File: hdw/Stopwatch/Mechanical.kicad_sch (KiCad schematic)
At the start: 12 parts

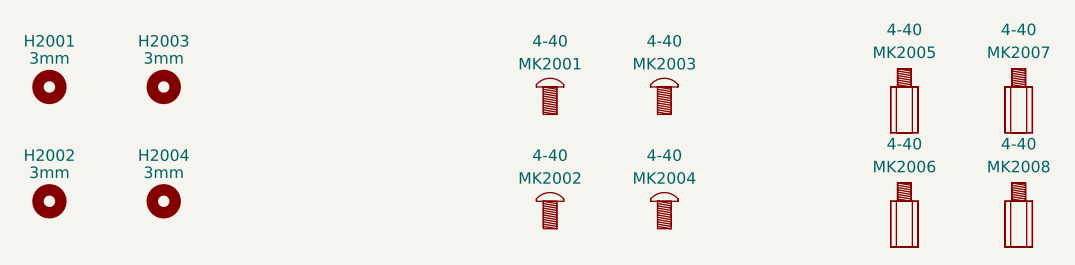
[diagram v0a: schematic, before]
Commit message: adjusted stage sheet
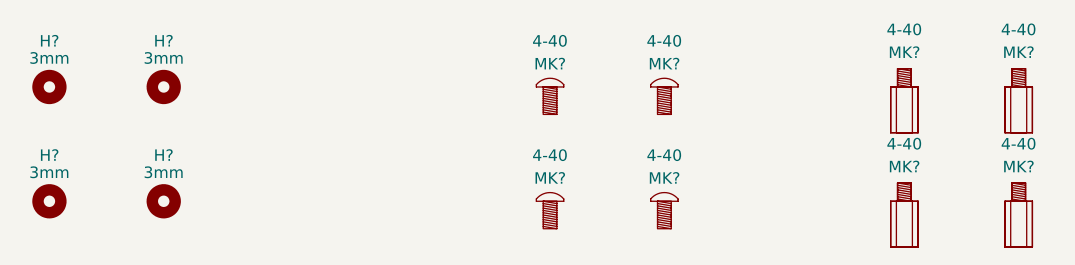
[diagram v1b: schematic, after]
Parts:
- renumbered H2001 to H?, H2003 to H?, H2002 to H?, H2004 to H?, MK2001 to MK?, MK2003 to MK?, MK2002 to MK?, MK2004 to MK?, MK2005 to MK?, MK2007 to MK?, MK2006 to MK?, MK2008 to MK?
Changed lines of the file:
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@@
   (symbol (lib_id "Mechanical:MountingHole") (at 42.164 44.45 0) (unit 1)
     (in_bom yes) (on_board yes) (dnp no)
-    (property "Reference" "H2001" (at 42.164 39.37 0)
+    (property "Reference" "H?" (at 42.164 39.37 0)
       (effects (font (size 1.27 1.27)))
     )
@@
       (project "Stopwatch"
         (path "/c0d2575b-aec2-49ed-8c32-97fe6e68824c/00000000-0000-0000-0000-00005d77c1ea"
-          (reference "H2001") (unit 1)
+          (reference "H?") (unit 1)
         )
       )
@@
   (symbol (lib_id "Mechanical:MountingHole") (at 54.864 44.45 0) (unit 1)
     (in_bom yes) (on_board yes) (dnp no)
-    (property "Reference" "H2003" (at 54.864 39.37 0)
+    (property "Reference" "H?" (at 54.864 39.37 0)
       (effects (font (size 1.27 1.27)))
     )
@@
       (project "Stopwatch"
         (path "/c0d2575b-aec2-49ed-8c32-97fe6e68824c/00000000-0000-0000-0000-00005d77c1ea"
-          (reference "H2003") (unit 1)
+          (reference "H?") (unit 1)
         )
       )
@@
   (symbol (lib_id "Mechanical:MountingHole") (at 42.164 57.15 0) (unit 1)
     (in_bom yes) (on_board yes) (dnp no)
-    (property "Reference" "H2002" (at 42.164 52.07 0)
+    (property "Reference" "H?" (at 42.164 52.07 0)
       (effects (font (size 1.27 1.27)))
     )
@@
       (project "Stopwatch"
         (path "/c0d2575b-aec2-49ed-8c32-97fe6e68824c/00000000-0000-0000-0000-00005d77c1ea"
-          (reference "H2002") (unit 1)
+          (reference "H?") (unit 1)
         )
       )
@@
   (symbol (lib_id "Mechanical:MountingHole") (at 54.864 57.15 0) (unit 1)
     (in_bom yes) (on_board yes) (dnp no)
-    (property "Reference" "H2004" (at 54.864 52.07 0)
+    (property "Reference" "H?" (at 54.864 52.07 0)
       (effects (font (size 1.27 1.27)))
     )
@@
       (project "Stopwatch"
         (path "/c0d2575b-aec2-49ed-8c32-97fe6e68824c/00000000-0000-0000-0000-00005d77c1ea"
-          (reference "H2004") (unit 1)
+          (reference "H?") (unit 1)
         )
       )
@@
   (symbol (lib_id "Custom_Library:Screw") (at 97.79 44.45 0) (unit 1)
     (in_bom yes) (on_board yes) (dnp no)
-    (property "Reference" "MK2001" (at 97.79 41.91 0)
+    (property "Reference" "MK?" (at 97.79 41.91 0)
       (effects (font (size 1.27 1.27)))
     )
@@
       (project "Stopwatch"
         (path "/c0d2575b-aec2-49ed-8c32-97fe6e68824c/00000000-0000-0000-0000-00005d77c1ea"
-          (reference "MK2001") (unit 1)
+          (reference "MK?") (unit 1)
         )
       )
@@
   (symbol (lib_id "Custom_Library:Screw") (at 110.49 44.45 0) (unit 1)
     (in_bom yes) (on_board yes) (dnp no)
-    (property "Reference" "MK2003" (at 110.49 41.91 0)
+    (property "Reference" "MK?" (at 110.49 41.91 0)
       (effects (font (size 1.27 1.27)))
     )
@@
       (project "Stopwatch"
         (path "/c0d2575b-aec2-49ed-8c32-97fe6e68824c/00000000-0000-0000-0000-00005d77c1ea"
-          (reference "MK2003") (unit 1)
+          (reference "MK?") (unit 1)
         )
       )
@@
   (symbol (lib_id "Custom_Library:Screw") (at 97.79 57.15 0) (unit 1)
     (in_bom yes) (on_board yes) (dnp no)
-    (property "Reference" "MK2002" (at 97.79 54.61 0)
+    (property "Reference" "MK?" (at 97.79 54.61 0)
       (effects (font (size 1.27 1.27)))
     )
@@
       (project "Stopwatch"
         (path "/c0d2575b-aec2-49ed-8c32-97fe6e68824c/00000000-0000-0000-0000-00005d77c1ea"
-          (reference "MK2002") (unit 1)
+          (reference "MK?") (unit 1)
         )
       )
@@
   (symbol (lib_id "Custom_Library:Screw") (at 110.49 57.15 0) (unit 1)
     (in_bom yes) (on_board yes) (dnp no)
-    (property "Reference" "MK2004" (at 110.49 54.61 0)
+    (property "Reference" "MK?" (at 110.49 54.61 0)
       (effects (font (size 1.27 1.27)))
     )
@@
       (project "Stopwatch"
         (path "/c0d2575b-aec2-49ed-8c32-97fe6e68824c/00000000-0000-0000-0000-00005d77c1ea"
-          (reference "MK2004") (unit 1)
+          (reference "MK?") (unit 1)
         )
       )
@@
   (symbol (lib_id "Custom_Library:Standoff") (at 137.16 44.45 0) (unit 1)
     (in_bom yes) (on_board yes) (dnp no)
-    (property "Reference" "MK2005" (at 137.16 40.64 0)
+    (property "Reference" "MK?" (at 137.16 40.64 0)
       (effects (font (size 1.27 1.27)))
     )
@@
       (project "Stopwatch"
         (path "/c0d2575b-aec2-49ed-8c32-97fe6e68824c/00000000-0000-0000-0000-00005d77c1ea"
-          (reference "MK2005") (unit 1)
+          (reference "MK?") (unit 1)
         )
       )
@@
   (symbol (lib_id "Custom_Library:Standoff") (at 149.86 44.45 0) (unit 1)
     (in_bom yes) (on_board yes) (dnp no)
-    (property "Reference" "MK2007" (at 149.86 40.64 0)
+    (property "Reference" "MK?" (at 149.86 40.64 0)
       (effects (font (size 1.27 1.27)))
     )
@@
       (project "Stopwatch"
         (path "/c0d2575b-aec2-49ed-8c32-97fe6e68824c/00000000-0000-0000-0000-00005d77c1ea"
-          (reference "MK2007") (unit 1)
+          (reference "MK?") (unit 1)
         )
       )
@@
   (symbol (lib_id "Custom_Library:Standoff") (at 137.16 57.15 0) (unit 1)
     (in_bom yes) (on_board yes) (dnp no)
-    (property "Reference" "MK2006" (at 137.16 53.34 0)
+    (property "Reference" "MK?" (at 137.16 53.34 0)
       (effects (font (size 1.27 1.27)))
     )
@@
       (project "Stopwatch"
         (path "/c0d2575b-aec2-49ed-8c32-97fe6e68824c/00000000-0000-0000-0000-00005d77c1ea"
-          (reference "MK2006") (unit 1)
+          (reference "MK?") (unit 1)
         )
       )
@@
   (symbol (lib_id "Custom_Library:Standoff") (at 149.86 57.15 0) (unit 1)
     (in_bom yes) (on_board yes) (dnp no)
-    (property "Reference" "MK2008" (at 149.86 53.34 0)
+    (property "Reference" "MK?" (at 149.86 53.34 0)
       (effects (font (size 1.27 1.27)))
     )
@@
       (project "Stopwatch"
         (path "/c0d2575b-aec2-49ed-8c32-97fe6e68824c/00000000-0000-0000-0000-00005d77c1ea"
-          (reference "MK2008") (unit 1)
-        )
-      )
+          (reference "MK?") (unit 1)
+        )
+      )

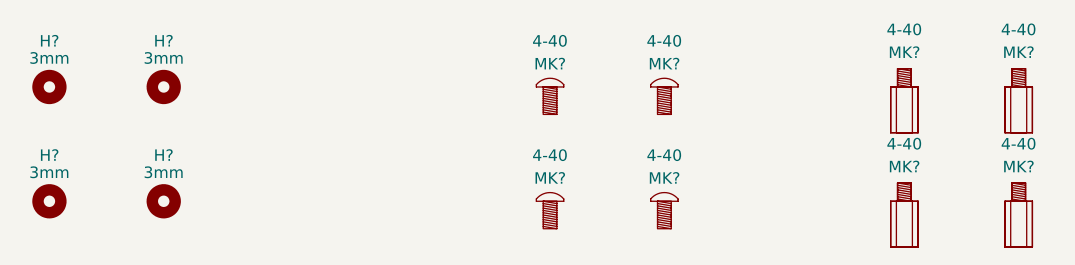
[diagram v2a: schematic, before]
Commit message: added proper power sequencing, discharge
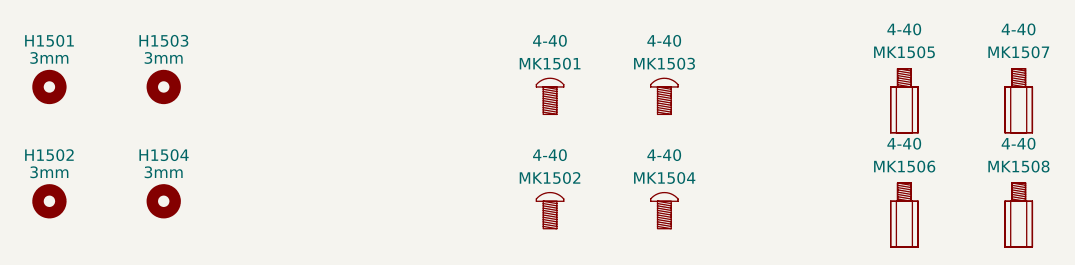
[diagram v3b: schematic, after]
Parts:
- gave numbers to parts that had none: 12
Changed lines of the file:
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@@
   (symbol (lib_id "Mechanical:MountingHole") (at 42.164 44.45 0) (unit 1)
     (in_bom yes) (on_board yes) (dnp no)
-    (property "Reference" "H?" (at 42.164 39.37 0)
+    (property "Reference" "H1501" (at 42.164 39.37 0)
       (effects (font (size 1.27 1.27)))
     )
@@
       (project "Stopwatch"
         (path "/c0d2575b-aec2-49ed-8c32-97fe6e68824c/00000000-0000-0000-0000-00005d77c1ea"
-          (reference "H?") (unit 1)
+          (reference "H1501") (unit 1)
         )
       )
@@
   (symbol (lib_id "Mechanical:MountingHole") (at 54.864 44.45 0) (unit 1)
     (in_bom yes) (on_board yes) (dnp no)
-    (property "Reference" "H?" (at 54.864 39.37 0)
+    (property "Reference" "H1503" (at 54.864 39.37 0)
       (effects (font (size 1.27 1.27)))
     )
@@
       (project "Stopwatch"
         (path "/c0d2575b-aec2-49ed-8c32-97fe6e68824c/00000000-0000-0000-0000-00005d77c1ea"
-          (reference "H?") (unit 1)
+          (reference "H1503") (unit 1)
         )
       )
@@
   (symbol (lib_id "Mechanical:MountingHole") (at 42.164 57.15 0) (unit 1)
     (in_bom yes) (on_board yes) (dnp no)
-    (property "Reference" "H?" (at 42.164 52.07 0)
+    (property "Reference" "H1502" (at 42.164 52.07 0)
       (effects (font (size 1.27 1.27)))
     )
@@
       (project "Stopwatch"
         (path "/c0d2575b-aec2-49ed-8c32-97fe6e68824c/00000000-0000-0000-0000-00005d77c1ea"
-          (reference "H?") (unit 1)
+          (reference "H1502") (unit 1)
         )
       )
@@
   (symbol (lib_id "Mechanical:MountingHole") (at 54.864 57.15 0) (unit 1)
     (in_bom yes) (on_board yes) (dnp no)
-    (property "Reference" "H?" (at 54.864 52.07 0)
+    (property "Reference" "H1504" (at 54.864 52.07 0)
       (effects (font (size 1.27 1.27)))
     )
@@
       (project "Stopwatch"
         (path "/c0d2575b-aec2-49ed-8c32-97fe6e68824c/00000000-0000-0000-0000-00005d77c1ea"
-          (reference "H?") (unit 1)
+          (reference "H1504") (unit 1)
         )
       )
@@
   (symbol (lib_id "Custom_Library:Screw") (at 97.79 44.45 0) (unit 1)
     (in_bom yes) (on_board yes) (dnp no)
-    (property "Reference" "MK?" (at 97.79 41.91 0)
+    (property "Reference" "MK1501" (at 97.79 41.91 0)
       (effects (font (size 1.27 1.27)))
     )
@@
       (project "Stopwatch"
         (path "/c0d2575b-aec2-49ed-8c32-97fe6e68824c/00000000-0000-0000-0000-00005d77c1ea"
-          (reference "MK?") (unit 1)
+          (reference "MK1501") (unit 1)
         )
       )
@@
   (symbol (lib_id "Custom_Library:Screw") (at 110.49 44.45 0) (unit 1)
     (in_bom yes) (on_board yes) (dnp no)
-    (property "Reference" "MK?" (at 110.49 41.91 0)
+    (property "Reference" "MK1503" (at 110.49 41.91 0)
       (effects (font (size 1.27 1.27)))
     )
@@
       (project "Stopwatch"
         (path "/c0d2575b-aec2-49ed-8c32-97fe6e68824c/00000000-0000-0000-0000-00005d77c1ea"
-          (reference "MK?") (unit 1)
+          (reference "MK1503") (unit 1)
         )
       )
@@
   (symbol (lib_id "Custom_Library:Screw") (at 97.79 57.15 0) (unit 1)
     (in_bom yes) (on_board yes) (dnp no)
-    (property "Reference" "MK?" (at 97.79 54.61 0)
+    (property "Reference" "MK1502" (at 97.79 54.61 0)
       (effects (font (size 1.27 1.27)))
     )
@@
       (project "Stopwatch"
         (path "/c0d2575b-aec2-49ed-8c32-97fe6e68824c/00000000-0000-0000-0000-00005d77c1ea"
-          (reference "MK?") (unit 1)
+          (reference "MK1502") (unit 1)
         )
       )
@@
   (symbol (lib_id "Custom_Library:Screw") (at 110.49 57.15 0) (unit 1)
     (in_bom yes) (on_board yes) (dnp no)
-    (property "Reference" "MK?" (at 110.49 54.61 0)
+    (property "Reference" "MK1504" (at 110.49 54.61 0)
       (effects (font (size 1.27 1.27)))
     )
@@
       (project "Stopwatch"
         (path "/c0d2575b-aec2-49ed-8c32-97fe6e68824c/00000000-0000-0000-0000-00005d77c1ea"
-          (reference "MK?") (unit 1)
+          (reference "MK1504") (unit 1)
         )
       )
@@
   (symbol (lib_id "Custom_Library:Standoff") (at 137.16 44.45 0) (unit 1)
     (in_bom yes) (on_board yes) (dnp no)
-    (property "Reference" "MK?" (at 137.16 40.64 0)
+    (property "Reference" "MK1505" (at 137.16 40.64 0)
       (effects (font (size 1.27 1.27)))
     )
@@
       (project "Stopwatch"
         (path "/c0d2575b-aec2-49ed-8c32-97fe6e68824c/00000000-0000-0000-0000-00005d77c1ea"
-          (reference "MK?") (unit 1)
+          (reference "MK1505") (unit 1)
         )
       )
@@
   (symbol (lib_id "Custom_Library:Standoff") (at 149.86 44.45 0) (unit 1)
     (in_bom yes) (on_board yes) (dnp no)
-    (property "Reference" "MK?" (at 149.86 40.64 0)
+    (property "Reference" "MK1507" (at 149.86 40.64 0)
       (effects (font (size 1.27 1.27)))
     )
@@
       (project "Stopwatch"
         (path "/c0d2575b-aec2-49ed-8c32-97fe6e68824c/00000000-0000-0000-0000-00005d77c1ea"
-          (reference "MK?") (unit 1)
+          (reference "MK1507") (unit 1)
         )
       )
@@
   (symbol (lib_id "Custom_Library:Standoff") (at 137.16 57.15 0) (unit 1)
     (in_bom yes) (on_board yes) (dnp no)
-    (property "Reference" "MK?" (at 137.16 53.34 0)
+    (property "Reference" "MK1506" (at 137.16 53.34 0)
       (effects (font (size 1.27 1.27)))
     )
@@
       (project "Stopwatch"
         (path "/c0d2575b-aec2-49ed-8c32-97fe6e68824c/00000000-0000-0000-0000-00005d77c1ea"
-          (reference "MK?") (unit 1)
+          (reference "MK1506") (unit 1)
         )
       )
@@
   (symbol (lib_id "Custom_Library:Standoff") (at 149.86 57.15 0) (unit 1)
     (in_bom yes) (on_board yes) (dnp no)
-    (property "Reference" "MK?" (at 149.86 53.34 0)
+    (property "Reference" "MK1508" (at 149.86 53.34 0)
       (effects (font (size 1.27 1.27)))
     )
@@
       (project "Stopwatch"
         (path "/c0d2575b-aec2-49ed-8c32-97fe6e68824c/00000000-0000-0000-0000-00005d77c1ea"
-          (reference "MK?") (unit 1)
-        )
-      )
+          (reference "MK1508") (unit 1)
+        )
+      )
